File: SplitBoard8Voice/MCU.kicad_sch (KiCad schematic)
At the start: 106 parts, among them J401 PWR, J402 DATA, J403 SWD Header, J404 MIDI_In, J405 Micro_SD_Card_Det2, J406 MIDI_Out, J407 MIDI_Thru, J408 POWER, SW401 RST, SW402 BOOT, U401 STM32F411RETx, U402 TPS56528DDA, U404 74HC04, U405 6N138, Y401 16MHz, Y402 32.768kHZ

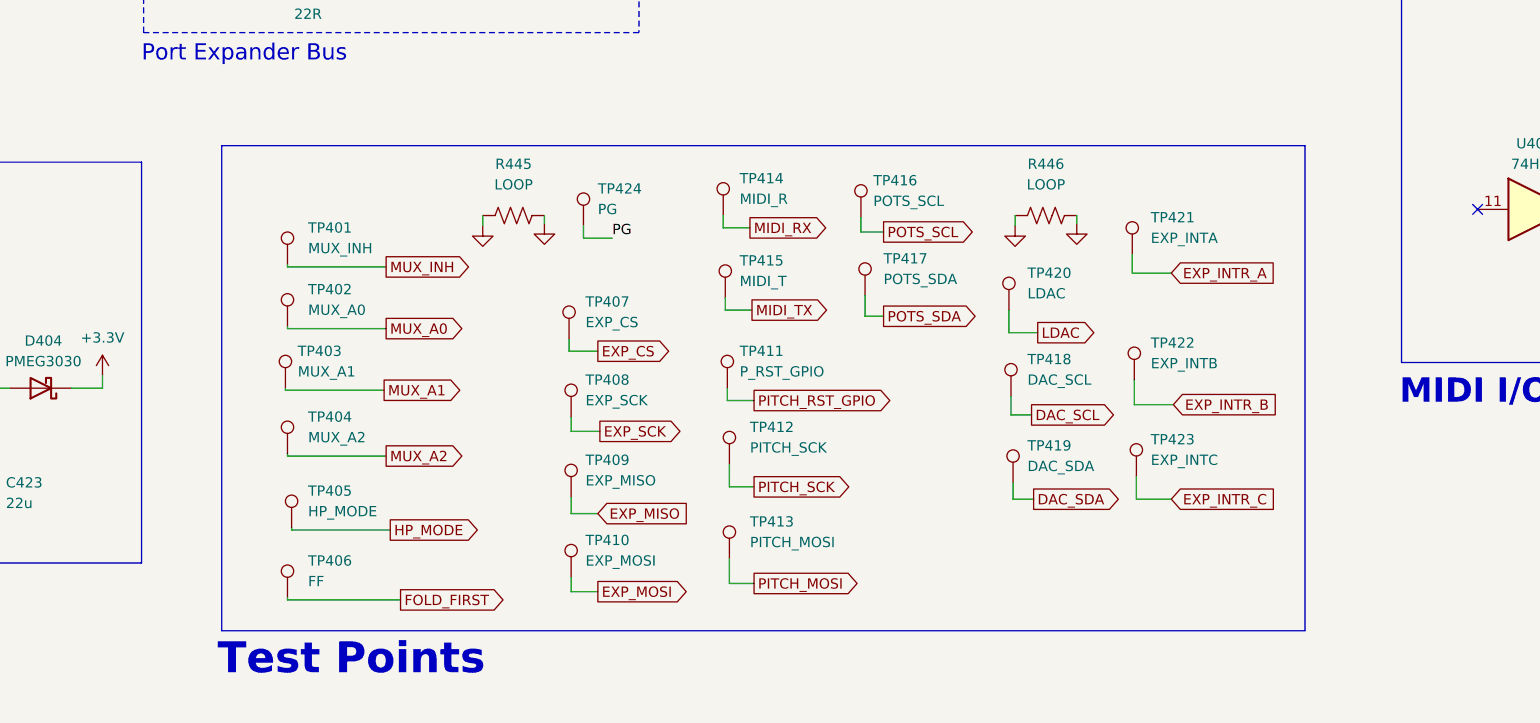
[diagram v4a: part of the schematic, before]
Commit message: ground pour and stitching vias
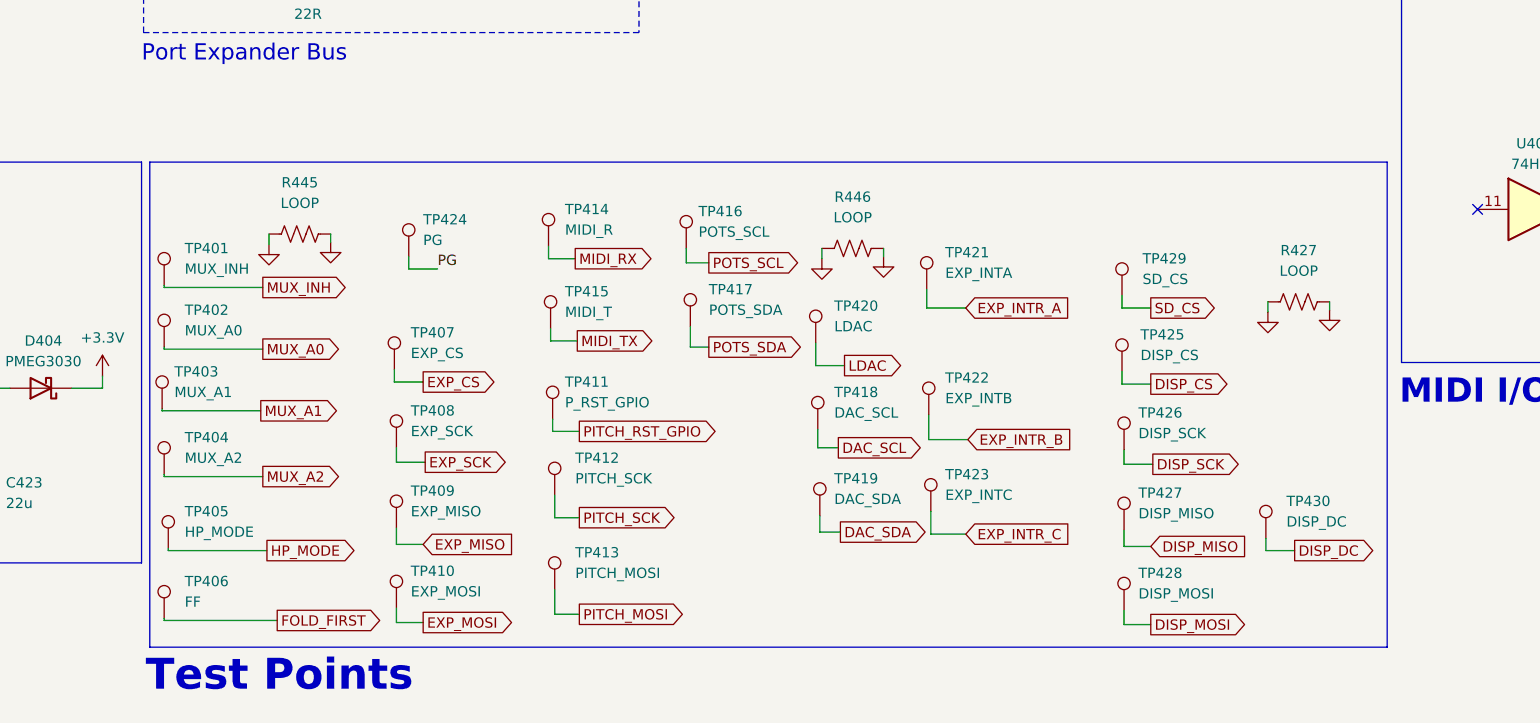
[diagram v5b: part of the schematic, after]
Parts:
- added R427: LOOP, Resistor_THT:R_Axial_DIN0204_L3.6mm_D1.6mm_P5.08mm_Horizontal, symbol Device:R_US
- added TP425: DISP_CS, TestPoint:TestPoint_THTPad_D1.0mm_Drill0.5mm_VAL, symbol Connector:TestPoint
- added TP426: DISP_SCK, TestPoint:TestPoint_THTPad_D1.0mm_Drill0.5mm_VAL, symbol Connector:TestPoint
- added TP427: DISP_MISO, TestPoint:TestPoint_THTPad_D1.0mm_Drill0.5mm_VAL, symbol Connector:TestPoint
- added TP428: DISP_MOSI, TestPoint:TestPoint_THTPad_D1.0mm_Drill0.5mm_VAL, symbol Connector:TestPoint
- added TP429: SD_CS, TestPoint:TestPoint_THTPad_D1.0mm_Drill0.5mm_VAL, symbol Connector:TestPoint
- added TP430: DISP_DC, TestPoint:TestPoint_THTPad_D1.0mm_Drill0.5mm_VAL, symbol Connector:TestPoint
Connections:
- net DISP_CS: now also TP425.1
- net DISP_DC: now also TP430.1
- net DISP_MISO: now also TP427.1
- net DISP_MOSI: now also TP428.1
- net DISP_SCK: now also TP426.1
- net GND: now also R427.1, R427.2
- net SD_CS: now also TP429.1
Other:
- moved on the sheet: R445, R446, TP401, TP402, TP403, TP404, TP405, TP406, TP407, TP408, TP409, TP410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
